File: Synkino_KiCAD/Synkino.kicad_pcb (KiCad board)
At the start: 2 copper layers, 88.4 x 82.3 mm, 180 parts, among them J1 Conn_01x02_Male, J10 EYE8_OUT, J11 EYE4_OUT, J12 2.5mm, J13 EYE5_OUT, J2 2.5mm, J3 3.5mm, J4 Micro_SD_Card_Det_Hirose_DM3AT, J5 EYE1_OUT, J6 EYE6_OUT, J7 EYE2_OUT, J8 EYE7_OUT, J9 EYE3_OUT, Q1 IRF7319, Q2 BC847, SW1 SW_Push, SW2 Rotary_Encoder_Switch, SW3 SW_Push, U1 MCP1702T-5002E/MB, U10 ATMEGA328P-AU, U11 QRE1113, U12 QRE1113, U13 QRE1113, U14 QRE1113, U15 QRE1113, U16 QRE1113, U18 QRE1113, U2 ATMEGA328P-AU, U3 74HC4050, U4 SPIOLED128x64, U5 AP7312-1833W6-7, U6 74HC14, U7 VS1053B, U8 MAX4741, U9 QRE1113, X1 FTDIconn, X2 ICSP, X3 FTDIconn, X4 ICSP, Y1 16Mhz, Y2 12.288MHz, Y3 16Mhz

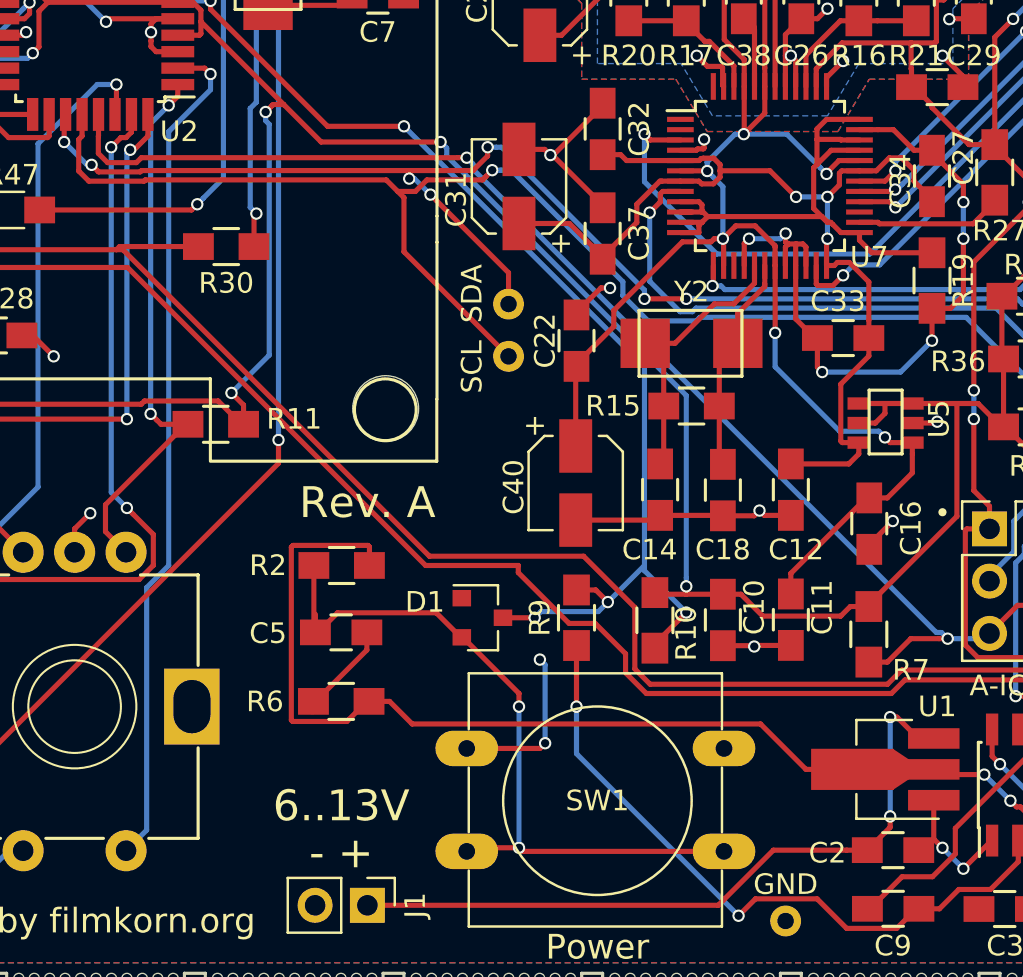
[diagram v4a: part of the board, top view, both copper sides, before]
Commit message: More Ground Planes, Make Pwr Button optional
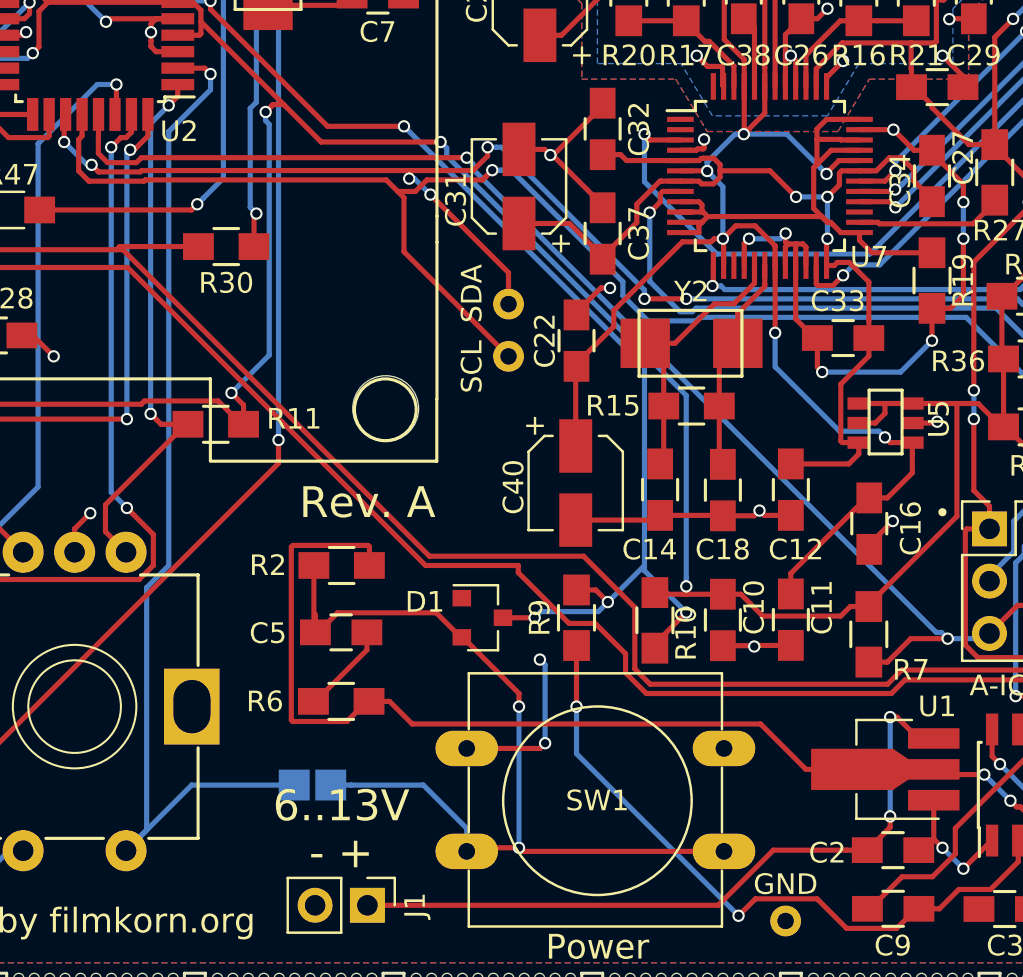
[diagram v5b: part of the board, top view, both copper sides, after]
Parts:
- added P.On1: P.On, Measurement_Points:Measurement_Point_Square-SMD-Pad_Small, B.Cu at (103.1, 98.3)
- added P.On2: P.On, Measurement_Points:Measurement_Point_Square-SMD-Pad_Small, B.Cu at (101.3, 98.3)
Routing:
- net Net-(P.On2-Pad1): track 41.1 -> 50.6 mm
- net Net-(C5-Pad2): track 36.2 -> 44.8 mm
- net GND: vias 49 -> 50

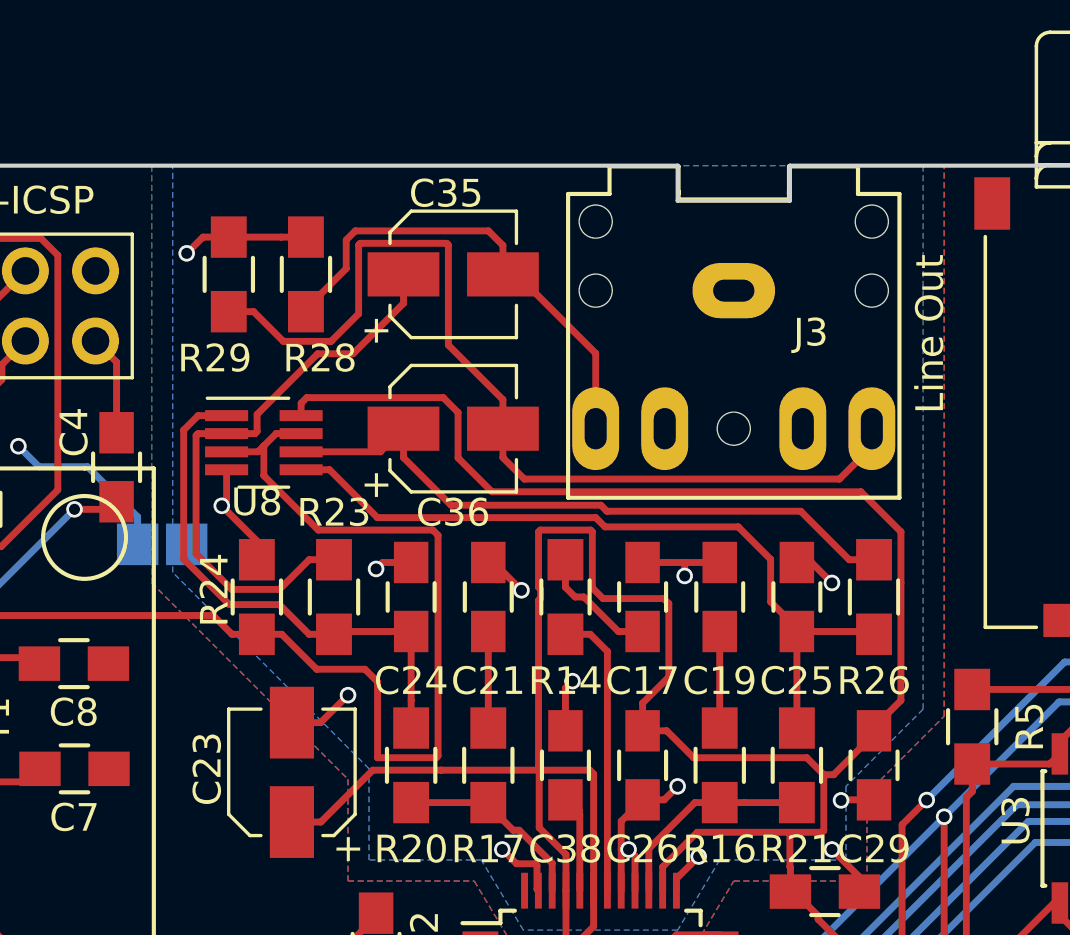
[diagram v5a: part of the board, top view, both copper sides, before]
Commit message: Adapt for wider MAX4741 version (cheaper)
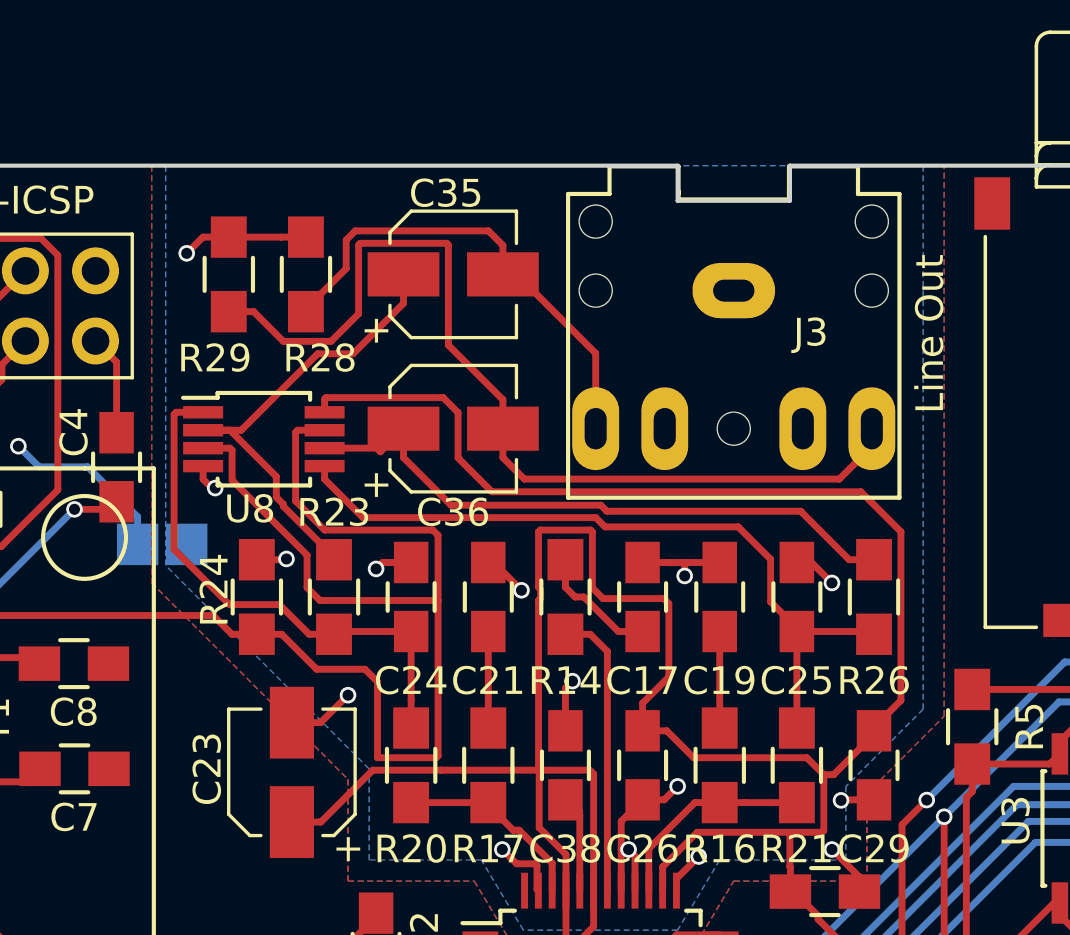
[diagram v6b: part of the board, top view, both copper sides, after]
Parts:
- U8: footprint TO_SOT_Packages_SMD:SOT-23-8_Handsoldering -> Housings_SSOP:MSOP-8_3x3mm_Pitch0.65mm
- moved U8 0.13 mm to (112.3, 48.0)
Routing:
- net /AUD_EN: track 50.0 -> 60.1 mm
- net Net-(C35-Pad1): track 21.2 -> 17.4 mm
- net GNDA: track 34.7 -> 33.0 mm, vias 14 -> 15
- net +3V3: track 219.8 -> 218.9 mm
- net Net-(C36-Pad1): track 23.7 -> 22.9 mm
- net Net-(C25-Pad1): track 27.7 -> 27.2 mm

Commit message: Kalle safe :)
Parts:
- moved GND 23.0 mm to (125.0, 67.1)
- moved GNDA 20.5 mm to (125.0, 65.3)
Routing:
- net GND: track 210.1 -> 203.8 mm, vias 50 -> 49
- net (no net): vias 0 -> 1
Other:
- board text added: "Rev. B"
- board text removed: "Rev. A"
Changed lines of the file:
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@@
     (links 372)
     (no_connects 0)
-    (area 71.552999 38.024999 160.095001 120.471001)
+    (area 62.682429 32.843999 168.838572 132.270286)
     (thickness 1.6)
     (drawings 82)
-    (tracks 2046)
+    (tracks 2043)
     (zones 0)
     (modules 182)
@@
   )
   (module Measurement_Points:Measurement_Point_Square-SMD-Pad_Small (layer B.Cu)
-    (at 107.696 51.816)
+    (at 124.968 67.056)
     (descr "Mesurement Point, Square, SMD Pad,  1.5mm x 1.5mm,")
     (tags "Mesurement Point Square SMD Pad 1.5x1.5mm")
     (attr virtual)
-    (fp_text reference GND (at 1.524 1.778) (layer B.SilkS)
+    (fp_text reference GND (at 2.54 -0.762) (layer B.SilkS)
       (effects (font (size 1 1) (thickness 0.15)) (justify mirror))
     )
-    (fp_text value GND (at 1.524 1.778) (layer B.Fab)
+    (fp_text value GND (at 2.54 -0.762) (layer B.Fab)
       (effects (font (size 1 1) (thickness 0.15)) (justify mirror))
     )
@@
   )
   (module Measurement_Points:Measurement_Point_Square-SMD-Pad_Small (layer B.Cu)
-    (at 109.474 51.816)
+    (at 124.968 65.278)
     (descr "Mesurement Point, Square, SMD Pad,  1.5mm x 1.5mm,")
     (tags "Mesurement Point Square SMD Pad 1.5x1.5mm")
@@
     (tags "SSOP 0.65")
     (attr smd)
-    (fp_text reference U8 (at -0.508 2.54) (layer F.SilkS)
+    (fp_text reference U8 (at -0.762 2.794) (layer F.SilkS)
       (effects (font (size 1 1) (thickness 0.15)))
     )
@@
     (effects (font (size 1.2 1.2) (thickness 0.25)) (justify mirror))
   )
-  (gr_text "Rev. A" (at 104.902 84.582) (layer F.SilkS)
+  (gr_text "Rev. B" (at 104.902 84.582) (layer F.SilkS)
     (effects (font (size 1.5 1.5) (thickness 0.3)))
   )
@@
   (gr_line (start 127.254 39.37) (end 131.318 39.37) (layer Edge.Cuts) (width 0.15))
   (gr_line (start 127.254 38.1) (end 127.254 39.37) (layer Edge.Cuts) (width 0.15))
+  (via (at 103.378 48.26) (size 0.6) (drill 0.4) (layers F.Cu B.Cu) (net 0))
   (segment (start 88.190005 60.575002) (end 88.490004 60.275003) (width 0.25) (layer B.Cu) (net 1))
   (via (at 88.490004 60.275003) (size 0.6) (drill 0.4) (layers F.Cu B.Cu) (net 1))
@@
   (segment (start 131.459 67.457) (end 130.459 66.457) (width 0.25) (layer F.Cu) (net 2))
   (via (at 130.459 66.457) (size 0.6) (drill 0.4) (layers F.Cu B.Cu) (net 2))
-  (segment (start 105.885792 49.005792) (end 104.123792 49.005792) (width 0.25) (layer B.Cu) (net 2))
-  (segment (start 104.123792 49.005792) (end 103.378 48.26) (width 0.25) (layer B.Cu) (net 2))
-  (via (at 103.378 48.26) (size 0.6) (drill 0.4) (layers F.Cu B.Cu) (net 2))
-  (segment (start 107.696 51.816) (end 107.696 50.816) (width 0.25) (layer B.Cu) (net 2))
-  (segment (start 107.696 50.816) (end 105.885792 49.005792) (width 0.25) (layer B.Cu) (net 2))
   (segment (start 87.884 54.356) (end 90.17 54.356) (width 0.25) (layer B.Cu) (net 2))
   (segment (start 90.17 54.356) (end 90.678 53.848) (width 0.25) (layer B.Cu) (net 2))
@@
   (segment (start 133.636001 103.370999) (end 132.696 104.311) (width 0.25) (layer F.Cu) (net 13))
   (segment (start 132.696 104.311) (end 131.696 104.311) (width 0.25) (layer F.Cu) (net 13))
+  (segment (start 123.19 66.675) (end 123.19 67.363002) (width 0.25) (layer B.Cu) (net 14))
+  (segment (start 123.19 67.363002) (end 124.434002 68.607004) (width 0.25) (layer B.Cu) (net 14))
+  (segment (start 124.434002 68.607004) (end 126.785725 68.607004) (width 0.25) (layer B.Cu) (net 14))
+  (segment (start 126.785725 68.607004) (end 127.209989 68.607004) (width 0.25) (layer B.Cu) (net 14))
   (segment (start 114.468 47.031) (end 114.468 46.556) (width 0.25) (layer F.Cu) (net 14))
   (segment (start 114.468 46.556) (end 114.524001 46.499999) (width 0.25) (layer F.Cu) (net 14))
@@
   (segment (start 122.174 69.228467) (end 121.711554 68.766021) (width 0.25) (layer B.Cu) (net 14))
   (segment (start 128.81 67.957) (end 127.813587 67.957) (width 0.25) (layer F.Cu) (net 14))
-  (segment (start 126.90999 68.307005) (end 127.209989 68.607004) (width 0.25) (layer B.Cu) (net 14))
-  (segment (start 123.19 66.675) (end 125.277985 66.675) (width 0.25) (layer B.Cu) (net 14))
-  (segment (start 127.813587 67.957) (end 127.209989 68.560598) (width 0.25) (layer F.Cu) (net 14))
-  (segment (start 127.209989 68.560598) (end 127.209989 68.607004) (width 0.25) (layer F.Cu) (net 14))
   (via (at 127.209989 68.607004) (size 0.6) (drill 0.4) (layers F.Cu B.Cu) (net 14))
-  (segment (start 125.277985 66.675) (end 126.90999 68.307005) (width 0.25) (layer B.Cu) (net 14))
+  (segment (start 127.209989 68.560598) (end 127.209989 68.607004) (width 0.25) (layer F.Cu) (net 14))
+  (segment (start 127.813587 67.957) (end 127.209989 68.560598) (width 0.25) (layer F.Cu) (net 14))
   (segment (start 123.21 64.357) (end 123.21 66.655) (width 0.25) (layer F.Cu) (net 14))
   (segment (start 123.21 66.655) (end 123.19 66.675) (width 0.25) (layer F.Cu) (net 14))
@@
   (segment (start 127.434989 67.457) (end 126.746 68.145989) (width 0.25) (layer F.Cu) (net 56))
   (segment (start 126.746 68.145989) (end 126.584987 68.307002) (width 0.25) (layer F.Cu) (net 56))
+  (segment (start 126.584987 68.307002) (end 126.584987 70.287987) (width 0.25) (layer F.Cu) (net 56))
+  (segment (start 126.584987 70.287987) (end 127.254 70.957) (width 0.25) (layer F.Cu) (net 56))
   (segment (start 127.21 65.957) (end 126.746 66.421) (width 0.25) (layer F.Cu) (net 56))
   (segment (start 128.81 65.957) (end 127.21 65.957) (width 0.25) (layer F.Cu) (net 56))
   (segment (start 128.81 67.457) (end 127.434989 67.457) (width 0.25) (layer F.Cu) (net 56))
-  (segment (start 126.584987 70.287987) (end 127.254 70.957) (width 0.25) (layer F.Cu) (net 56))
-  (segment (start 126.584987 68.307002) (end 126.584987 70.287987) (width 0.25) (layer F.Cu) (net 56))
   (segment (start 127.41 70.957) (end 127.254 70.957) (width 0.25) (layer F.Cu) (net 56))
   (segment (start 120.11 70.457) (end 121.13 70.457) (width 0.25) (layer F.Cu) (net 56))
